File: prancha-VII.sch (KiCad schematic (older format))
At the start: 0 parts

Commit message: conector de 70 pinos para a interconexão das placas e término do desenho da prancha 5.
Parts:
- added P?: CONN_35X2, symbol CONN_35X2
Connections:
- new net ?: P?.1 (P1), P?.10 (P10), P?.11 (P11), P?.12 (P12), P?.13 (P13), P?.14 (P14), P?.15 (P15), P?.16 (P16), P?.17 (P17), P?.18 (P18), P?.19 (P19), P?.2 (P2), P?.20 (P20), P?.21 (P21), P?.22 (P22), P?.23 (P23), P?.24 (P24), P?.25, P?.26 (P26), P?.27 (P27), P?.28 (P28), P?.29 (P29), P?.3 (P3), P?.30 (P30), P?.31 (P31), P?.32 (P32), P?.33 (P33), P?.34 (P34), P?.35 (P35), P?.36 (P36), P?.37 (P37), P?.38 (P38), P?.39 (P39), P?.4 (P4), P?.40 (P40), P?.41 (P41), P?.42 (P42), P?.43 (P43), P?.44 (P44), P?.45 (P45), P?.46 (P46), P?.47 (P47), P?.48 (P48), P?.49 (P49), P?.5 (P5), P?.50 (P50), P?.51 (P51), P?.52 (P52), P?.53 (P53), P?.54 (P54), P?.55 (P55), P?.56 (P56), P?.57 (P57), P?.58 (P58), P?.59 (P59), P?.6 (P6), P?.60 (P60), P?.61 (P61), P?.62 (P62), P?.63 (P63), P?.64 (P64), P?.65 (P65), P?.66 (P66), P?.67 (P67), P?.68 (P68), P?.69 (P69), P?.7 (P7), P?.70 (P70), P?.8 (P8), P?.9 (P9)

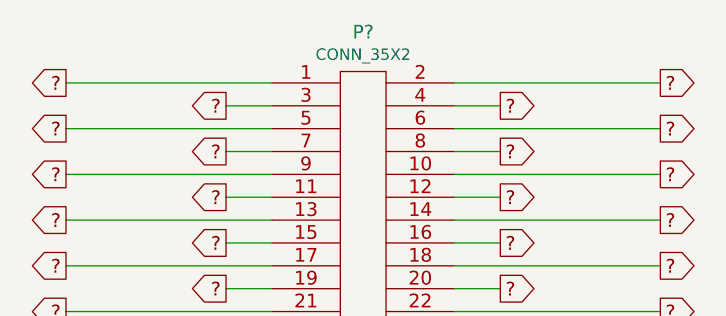
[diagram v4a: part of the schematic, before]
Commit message: numerando todas referencias e corrigindo erros de referencias duplas ou pacotes inconsistentes
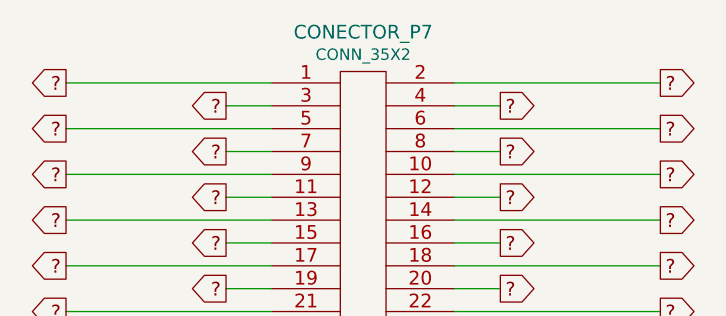
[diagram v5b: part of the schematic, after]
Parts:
- gave numbers to parts that had none: 1
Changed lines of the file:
@@
 $EndDescr
 $Comp
-L CONN_35X2 P?
+L CONN_35X2 CONECTOR_P7
 U 1 1 587C20A7
 P 2250 2700
-F 0 "P?" H 2250 4622 60  0000 C CNN
+F 0 "CONECTOR_P7" H 2250 4622 60  0000 C CNN
 F 1 "CONN_35X2" H 2250 4524 50  0000 C CNN
 F 2 "" H 2250 2950 60  0000 C CNN
